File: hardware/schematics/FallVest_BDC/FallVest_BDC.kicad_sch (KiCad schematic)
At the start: 1 part, among them U1 STM32WBA55HEFx

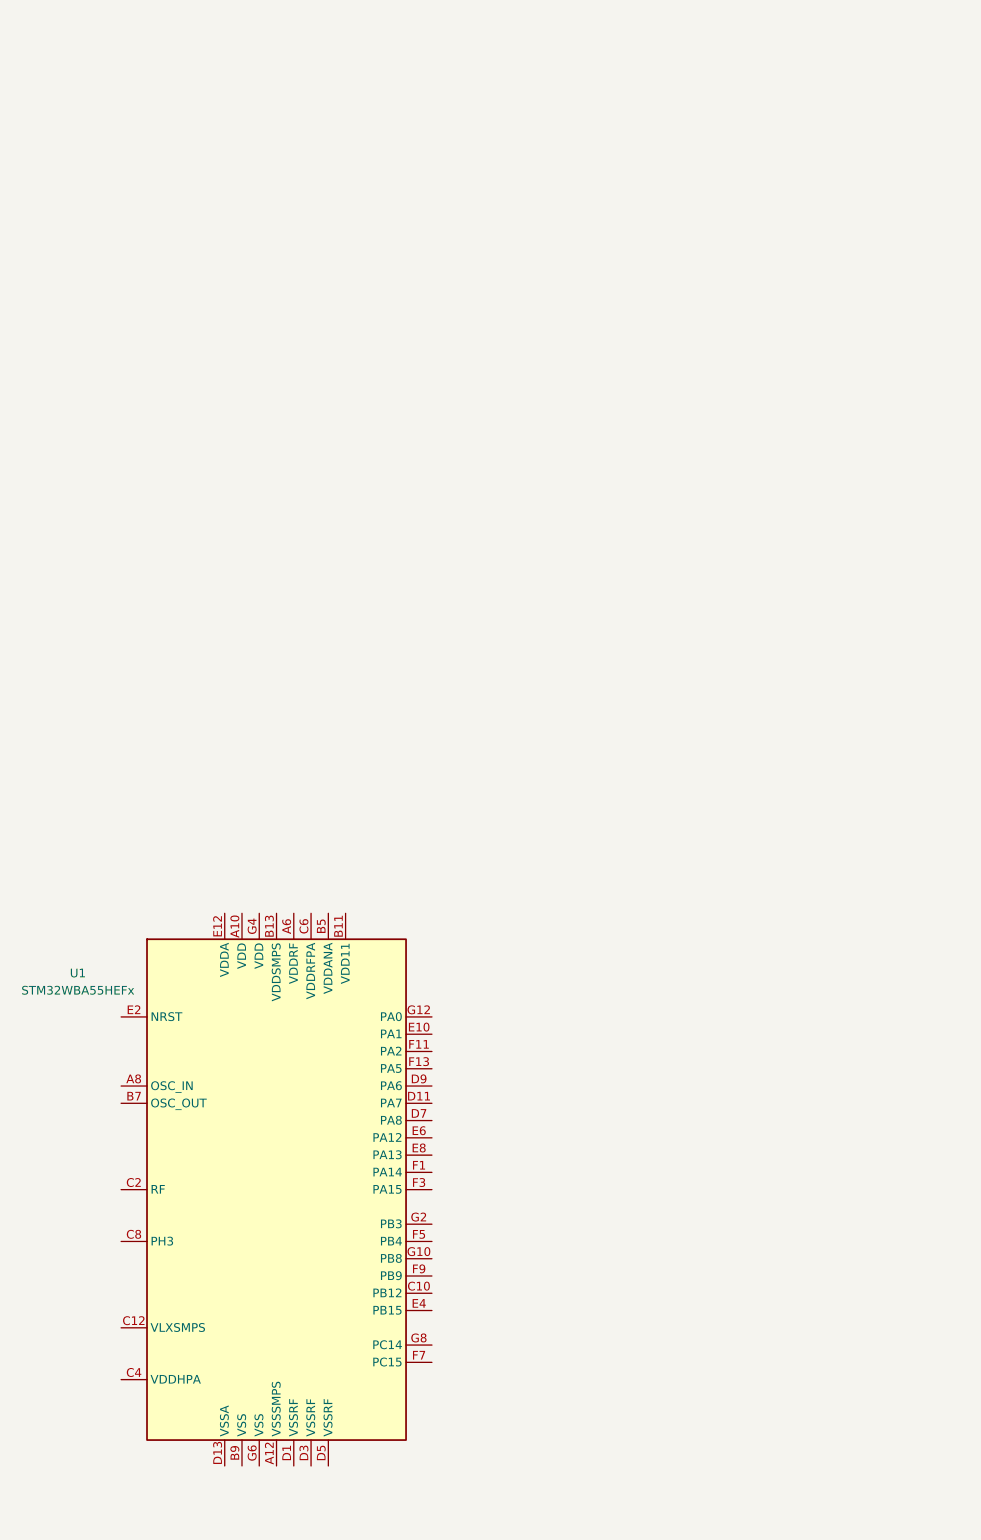
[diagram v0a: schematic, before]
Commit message: Adding parts to schem
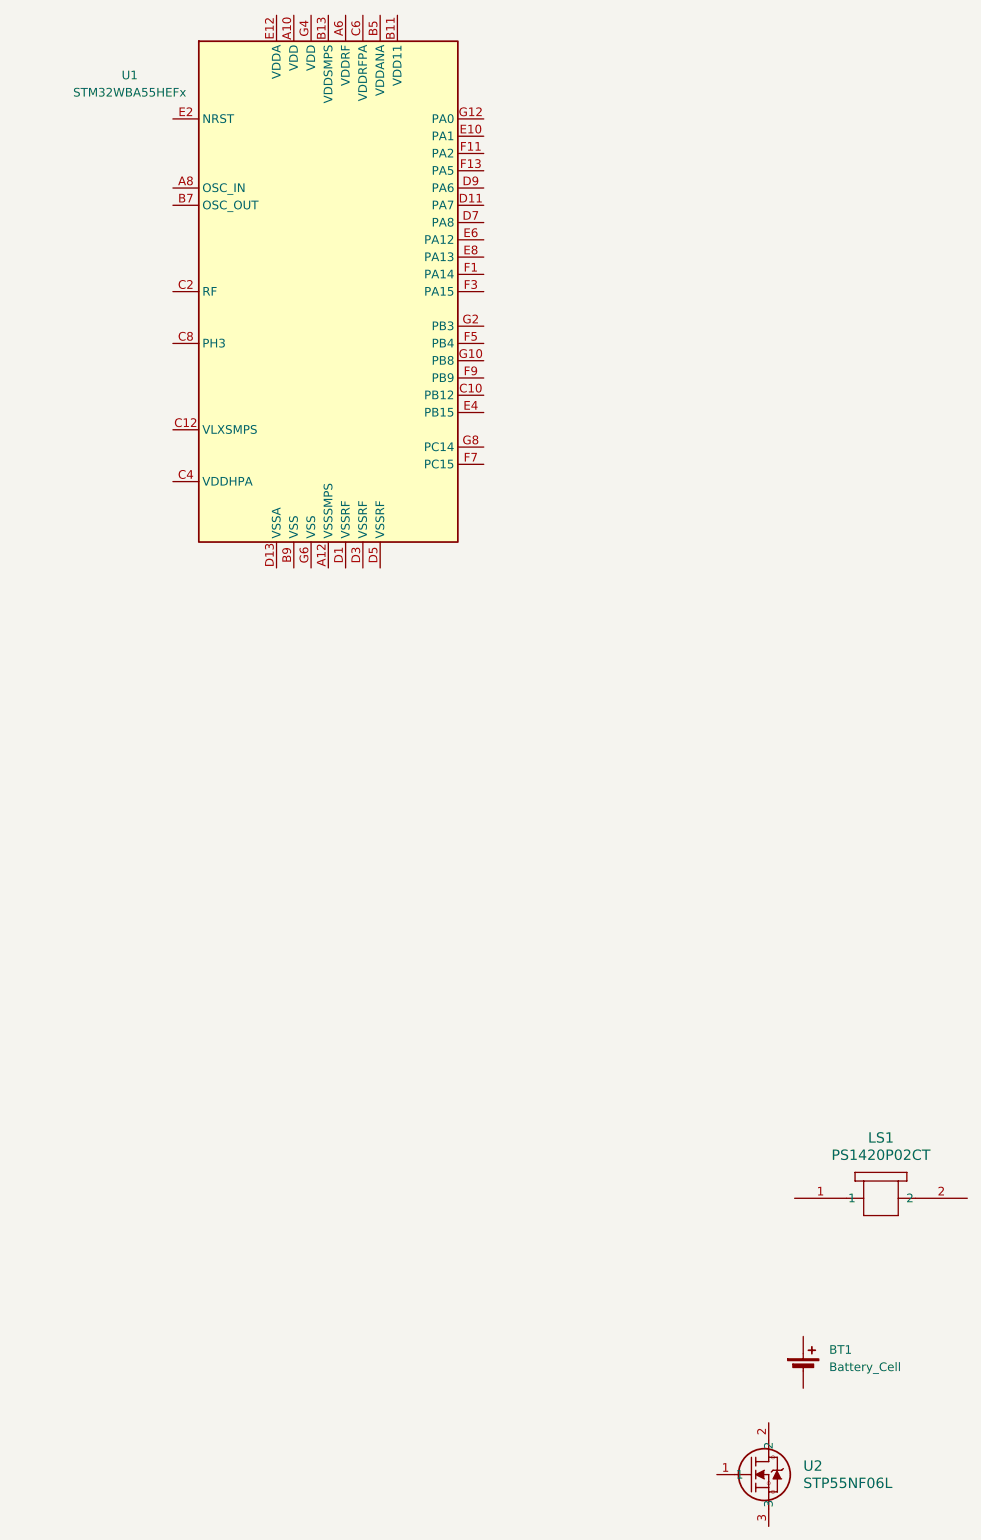
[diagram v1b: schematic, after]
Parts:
- added BT1: Battery_Cell, symbol Device:Battery_Cell
- added LS1: PS1420P02CT, PS1420P02CT_TDK, symbol 2026-09-14_03-29-42:PS1420P02CT
- added U2: STP55NF06L, TO-220_STM, symbol EE_VEST_SYM:STP55NF06L
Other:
- moved on the sheet: U1

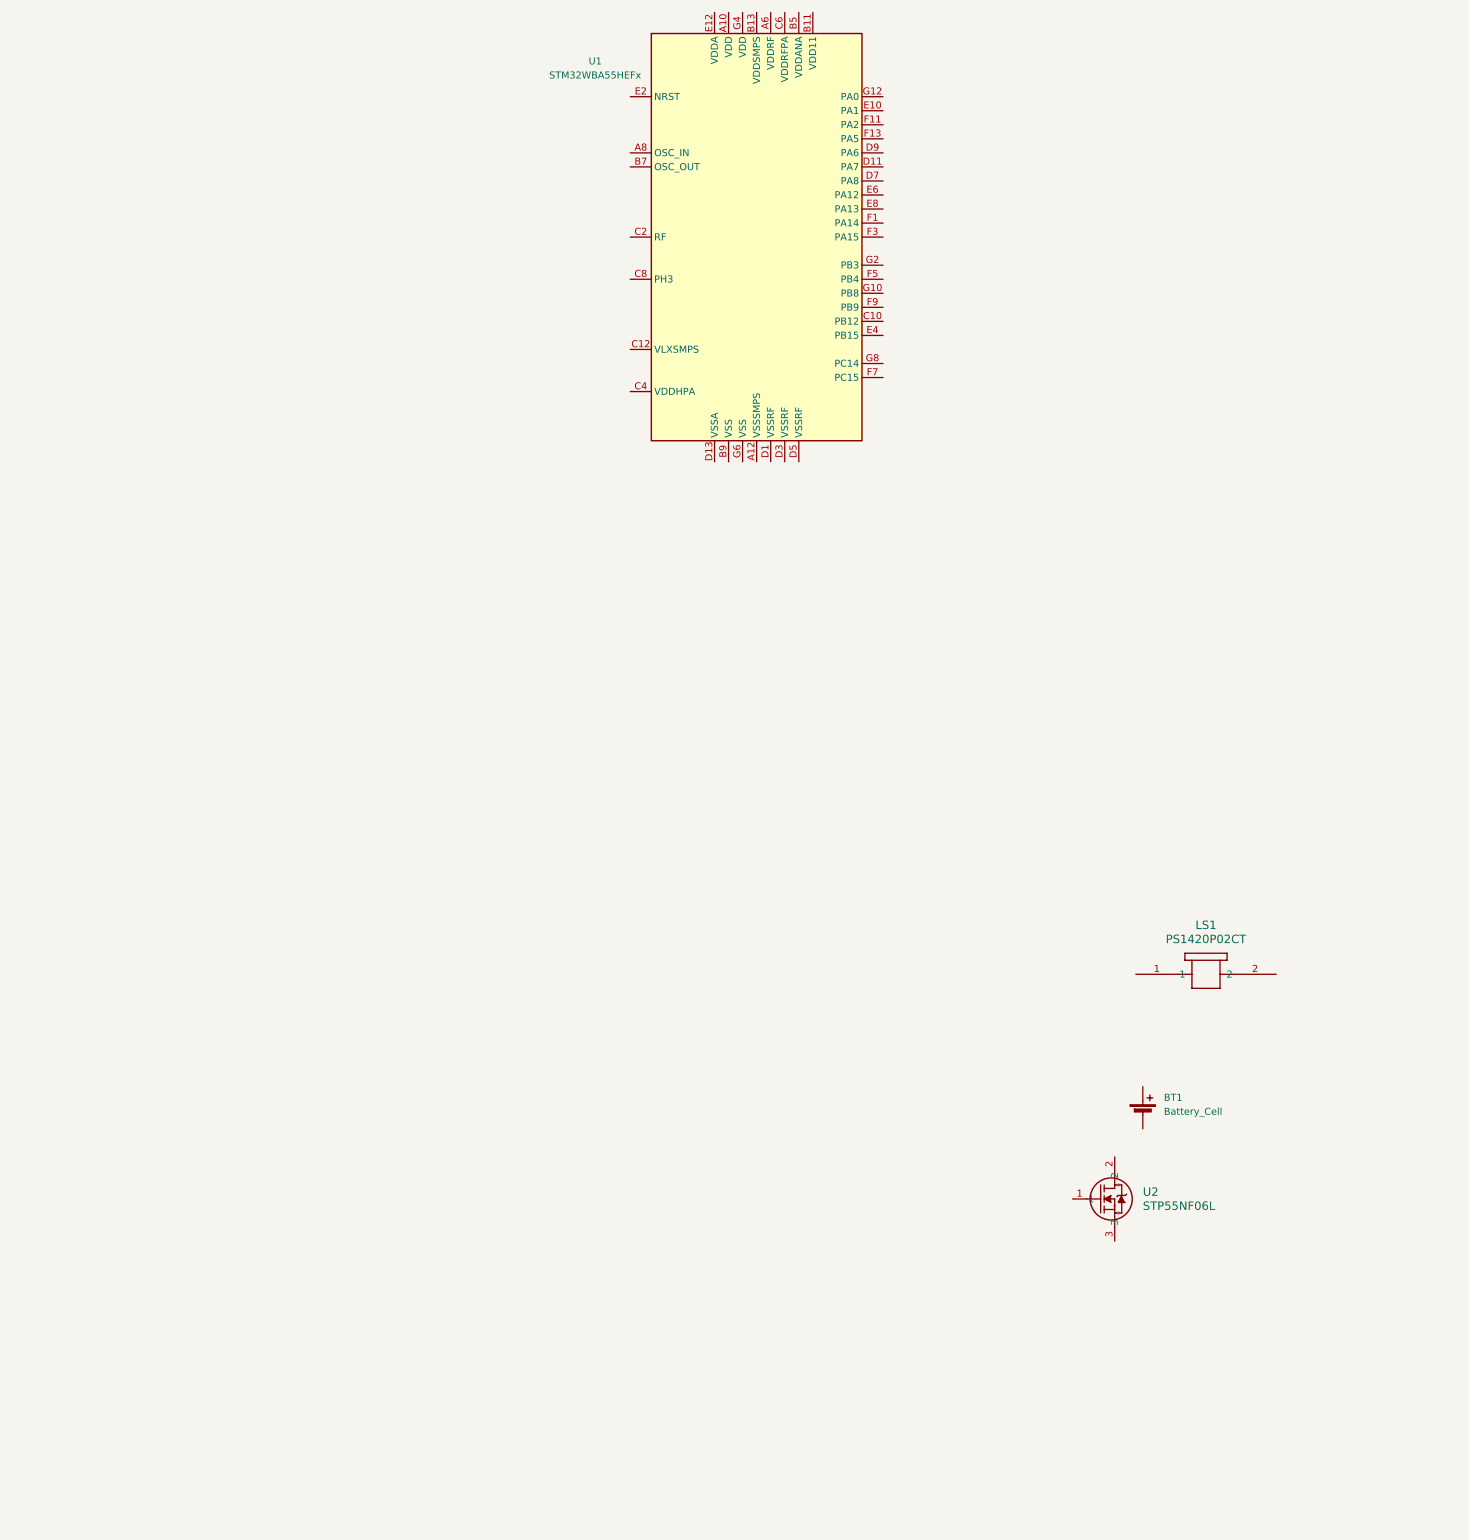
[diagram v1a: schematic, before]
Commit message: Finished adding in parts for Schematic
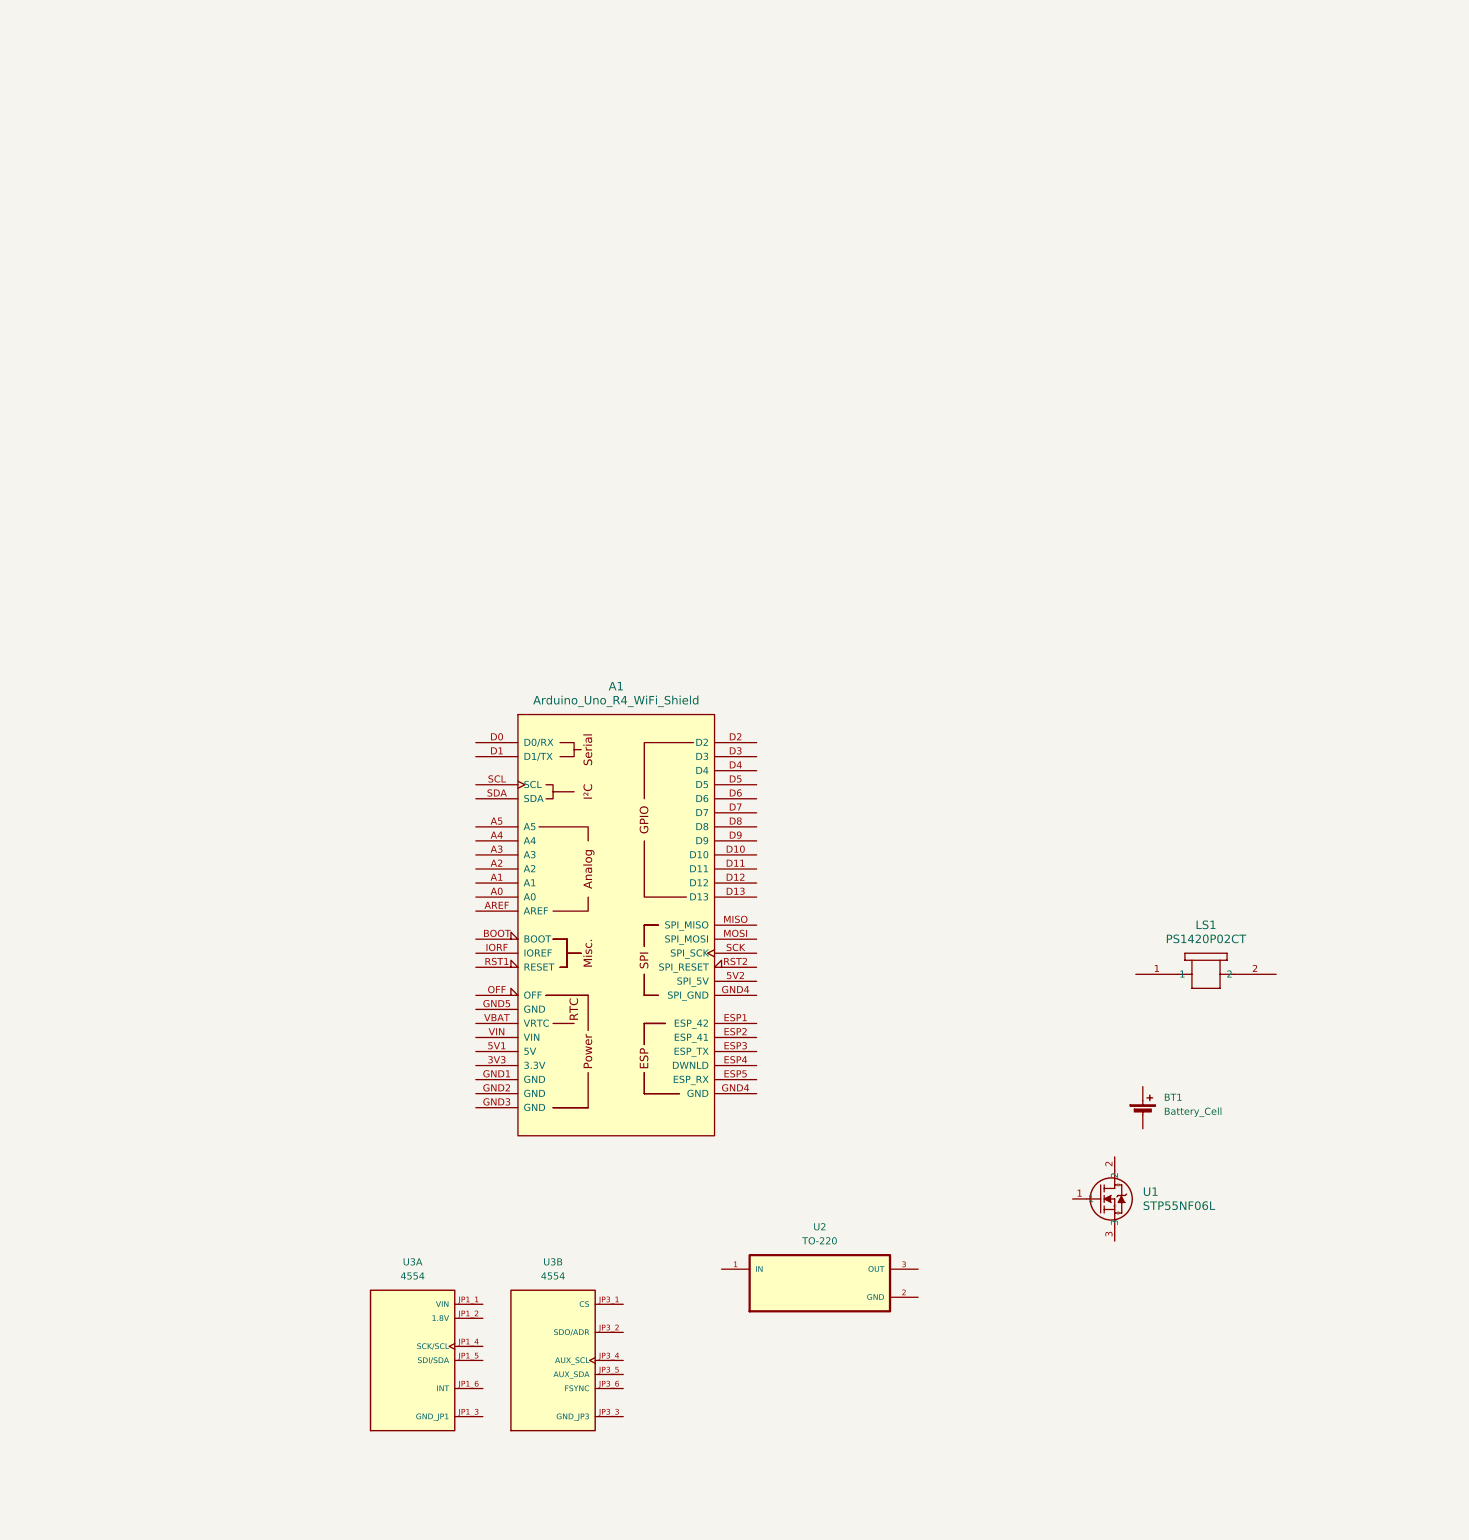
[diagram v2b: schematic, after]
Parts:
- removed U1: STM32WBA55HEFx, Package_CSP:ST_WLCSP-41_2.98x2.76mm_Layout13x7_P0.4mm_Stagger, symbol MCU_ST_STM32WB:STM32WBA55HEFx
- added A1: Arduino_Uno_R4_WiFi_Shield, PCM_arduino-library:Arduino_Uno_R4_WiFi_Shield, symbol arduino-library:Arduino_Uno_R4_WiFi_Shield
- added U2: TO-220, LM3940IT-3.3:TO254P1054X470X1955-3, symbol EE_VEST_SYM:TO-220_3.3V-Reg
- added U3: 4554, 4554:MODULE_4554, symbol EE_VEST_SYM:4554
- renumbered U2 to U1
